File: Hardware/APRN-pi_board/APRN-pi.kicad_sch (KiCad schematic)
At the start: 30 parts, among them J1 Raspberry_Pi_2_3, J2 Conn_Coaxial, J3 Amplifier Jumper, J4 Screw_Terminal_01x02, J5 AudioJack4, Q1 MMBT3906, U1 DRA818V, U2 L7805

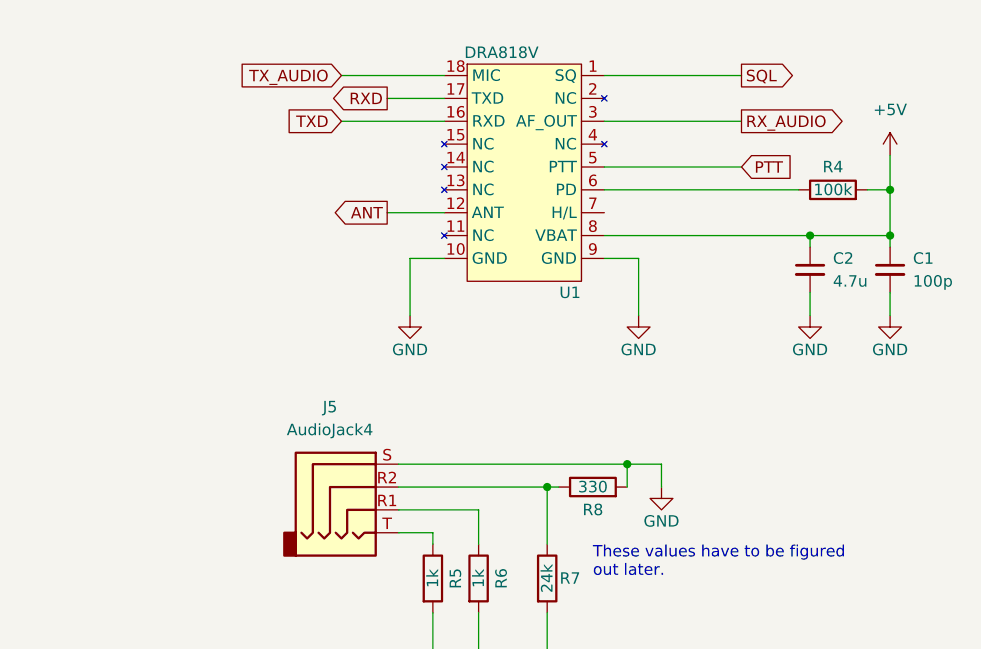
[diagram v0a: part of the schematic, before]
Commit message: Add h/l jumper
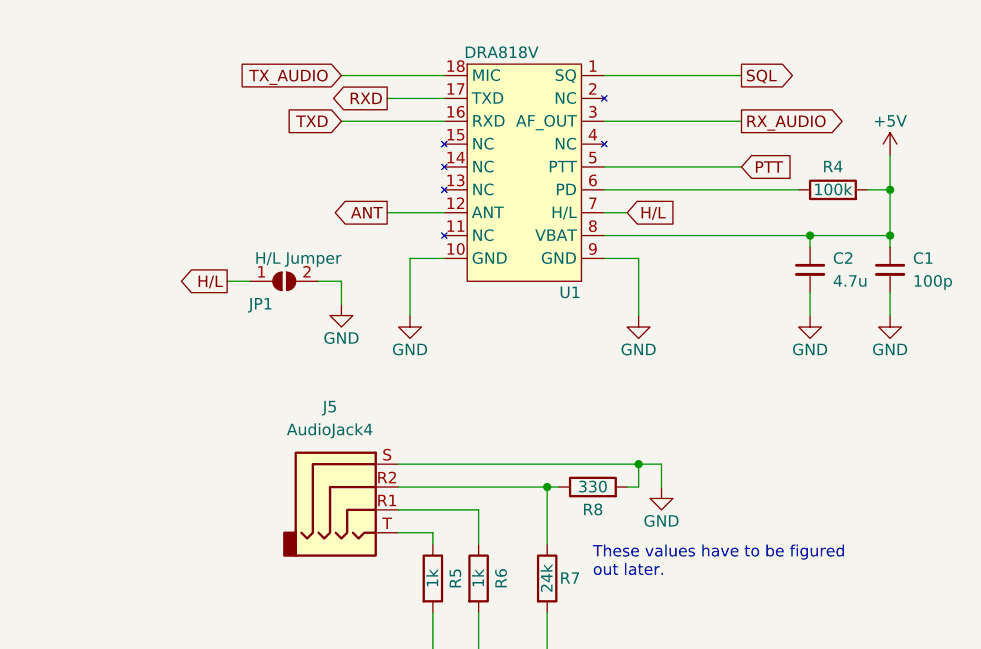
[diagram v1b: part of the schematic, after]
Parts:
- added JP1: H/L Jumper, Jumper:SolderJumper-2_P1.3mm_Open_TrianglePad1.0x1.5mm, symbol Jumper:SolderJumper_2_Open
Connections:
- net GND: now also JP1.2 (B)
- net H/L: now reaches U1.7 (H/L)
- net H/L: now also JP1.1 (A)
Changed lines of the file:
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@@
   (junction (at 76.2 97.79) (diameter 0) (color 0 0 0 0)
   )
-  (junction (at 245.11 64.77) (diameter 0) (color 0 0 0 0)
-  )
   (junction (at 33.02 97.79) (diameter 0) (color 0 0 0 0)
   )
@@
   )
   (junction (at 152.4 68.58) (diameter 0) (color 0 0 0 0)
+  )
+  (junction (at 246.38 64.77) (diameter 0) (color 0 0 0 0)
   )
   (junction (at 265.43 39.37) (diameter 0) (color 0 0 0 0)
@@
     (stroke (width 0) (type default) (color 0 0 0 0))
   )
+  (wire (pts (xy 246.38 64.77) (xy 248.92 64.77))
+    (stroke (width 0) (type default) (color 0 0 0 0))
+  )
   (wire (pts (xy 40.64 24.13) (xy 48.26 24.13))
     (stroke (width 0) (type default) (color 0 0 0 0))
@@
     (stroke (width 0) (type default) (color 0 0 0 0))
   )
+  (wire (pts (xy 242.57 36.83) (xy 245.11 36.83))
+    (stroke (width 0) (type default) (color 0 0 0 0))
+  )
   (wire (pts (xy 213.36 21.59) (xy 224.79 21.59))
     (stroke (width 0) (type default) (color 0 0 0 0))
@@
     (stroke (width 0) (type default) (color 0 0 0 0))
   )
-  (wire (pts (xy 219.71 64.77) (xy 245.11 64.77))
-    (stroke (width 0) (type default) (color 0 0 0 0))
-  )
   (wire (pts (xy 76.2 121.92) (xy 82.55 121.92))
     (stroke (width 0) (type default) (color 0 0 0 0))
@@
     (stroke (width 0) (type default) (color 0 0 0 0))
   )
+  (wire (pts (xy 213.36 44.45) (xy 213.36 46.99))
+    (stroke (width 0) (type default) (color 0 0 0 0))
+  )
   (wire (pts (xy 154.94 139.7) (xy 160.02 139.7))
     (stroke (width 0) (type default) (color 0 0 0 0))
@@
     (stroke (width 0) (type default) (color 0 0 0 0))
   )
+  (wire (pts (xy 210.82 44.45) (xy 213.36 44.45))
+    (stroke (width 0) (type default) (color 0 0 0 0))
+  )
   (wire (pts (xy 242.57 39.37) (xy 265.43 39.37))
     (stroke (width 0) (type default) (color 0 0 0 0))
@@
     (stroke (width 0) (type default) (color 0 0 0 0))
   )
+  (wire (pts (xy 246.38 67.31) (xy 245.11 67.31))
+    (stroke (width 0) (type default) (color 0 0 0 0))
+  )
   (wire (pts (xy 144.78 68.58) (xy 142.24 68.58))
     (stroke (width 0) (type default) (color 0 0 0 0))
@@
     (stroke (width 0) (type default) (color 0 0 0 0))
   )
+  (wire (pts (xy 219.71 64.77) (xy 246.38 64.77))
+    (stroke (width 0) (type default) (color 0 0 0 0))
+  )
   (wire (pts (xy 242.57 34.29) (xy 264.16 34.29))
     (stroke (width 0) (type default) (color 0 0 0 0))
@@
     (stroke (width 0) (type default) (color 0 0 0 0))
   )
-  (wire (pts (xy 245.11 64.77) (xy 248.92 64.77))
-    (stroke (width 0) (type default) (color 0 0 0 0))
-  )
   (wire (pts (xy 64.77 121.92) (xy 76.2 121.92))
     (stroke (width 0) (type default) (color 0 0 0 0))
@@
     (stroke (width 0) (type default) (color 0 0 0 0))
   )
-  (wire (pts (xy 245.11 64.77) (xy 245.11 67.31))
+  (wire (pts (xy 246.38 64.77) (xy 246.38 67.31))
+    (stroke (width 0) (type default) (color 0 0 0 0))
+  )
+  (wire (pts (xy 200.66 44.45) (xy 203.2 44.45))
     (stroke (width 0) (type default) (color 0 0 0 0))
   )
@@
     )
   )
+  (global_label "H{slash}L" (shape input) (at 245.11 36.83 0) (fields_autoplaced)
+    (effects (font (size 1.27 1.27)) (justify left))
+    (property "Intersheet References" "${INTERSHEET_REFS}" (id 0) (at 251.2121 36.7506 0)
+      (effects (font (size 1.27 1.27)) (justify left) hide)
+    )
+  )
   (global_label "PTT" (shape input) (at 257.81 31.75 0) (fields_autoplaced)
     (effects (font (size 1.27 1.27)) (justify left))
@@
     (effects (font (size 1.27 1.27)) (justify right))
     (property "Intersheet References" "${INTERSHEET_REFS}" (id 0) (at 212.6402 36.9094 0)
+      (effects (font (size 1.27 1.27)) (justify right) hide)
+    )
+  )
+  (global_label "H{slash}L" (shape output) (at 200.66 44.45 180) (fields_autoplaced)
+    (effects (font (size 1.27 1.27)) (justify right))
+    (property "Intersheet References" "${INTERSHEET_REFS}" (id 0) (at 194.5579 44.3706 0)
       (effects (font (size 1.27 1.27)) (justify right) hide)
     )
@@
   )
   (symbol (lib_id "power:+5V") (at 274.32 30.48 0) (unit 1)
-    (in_bom yes) (on_board yes) (fields_autoplaced)
+    (in_bom yes) (on_board yes)
     (property "Reference" "#PWR0104" (id 0) (at 274.32 34.29 0)
       (effects (font (size 1.27 1.27)) hide)
     )
-    (property "Value" "+5V" (id 1) (at 274.32 25.4 0))
+    (property "Value" "+5V" (id 1) (at 274.32 26.67 0))
     (property "Footprint" "" (id 2) (at 274.32 30.48 0)
       (effects (font (size 1.27 1.27)) hide)
@@
     (pin "1")
   )
+  (symbol (lib_id "Jumper:SolderJumper_2_Open") (at 207.01 44.45 0) (unit 1)
+    (in_bom yes) (on_board yes)
+    (property "Reference" "JP1" (id 0) (at 205.74 46.99 0)
+      (effects (font (size 1.27 1.27)) (justify right))
+    )
+    (property "Value" "H/L Jumper" (id 1) (at 213.36 41.91 0)
+      (effects (font (size 1.27 1.27)) (justify right))
+    )
+    (property "Footprint" "Jumper:SolderJumper-2_P1.3mm_Open_TrianglePad1.0x1.5mm" (id 2) (at 207.01 44.45 0)
+      (effects (font (size 1.27 1.27)) hide)
+    )
+    (property "Datasheet" "~" (id 3) (at 207.01 44.45 0)
+      (effects (font (size 1.27 1.27)) hide)
+    )
+    (pin "1")
+    (pin "2")
+  )
   (symbol (lib_id "Device:R") (at 50.8 97.79 90) (unit 1)
     (in_bom yes) (on_board yes)
@@
     )
     (property "Datasheet" "" (id 3) (at 220.98 48.26 0)
+      (effects (font (size 1.27 1.27)) hide)
+    )
+    (pin "1")
+  )
+  (symbol (lib_id "power:GND") (at 213.36 46.99 0) (unit 1)
+    (in_bom yes) (on_board yes)
+    (property "Reference" "#PWR01" (id 0) (at 213.36 53.34 0)
+      (effects (font (size 1.27 1.27)) hide)
+    )
+    (property "Value" "GND" (id 1) (at 213.36 50.8 0))
+    (property "Footprint" "" (id 2) (at 213.36 46.99 0)
+      (effects (font (size 1.27 1.27)) hide)
+    )
+    (property "Datasheet" "" (id 3) (at 213.36 46.99 0)
       (effects (font (size 1.27 1.27)) hide)
     )
@@
   )
   (symbol_instances
+    (path "/7a4a7cd3-b322-4799-bd04-d77279f4cccb"
+      (reference "#PWR01") (unit 1) (value "GND") (footprint "")
+    )
     (path "/154d3377-6296-4aab-9aa3-3cabfc82996f"
       (reference "#PWR0101") (unit 1) (value "GND") (footprint "")
@@
       (reference "J5") (unit 1) (value "AudioJack4") (footprint "Connector_Audio:Jack_3.5mm_PJ320E_Horizontal")
     )
+    (path "/67106f57-015d-42ff-af4d-a495d14e3d9c"
+      (reference "JP1") (unit 1) (value "H/L Jumper") (footprint "Jumper:SolderJumper-2_P1.3mm_Open_TrianglePad1.0x1.5mm")
+    )
     (path "/934fbbb7-68d4-48b2-b966-8b80b47dd229"

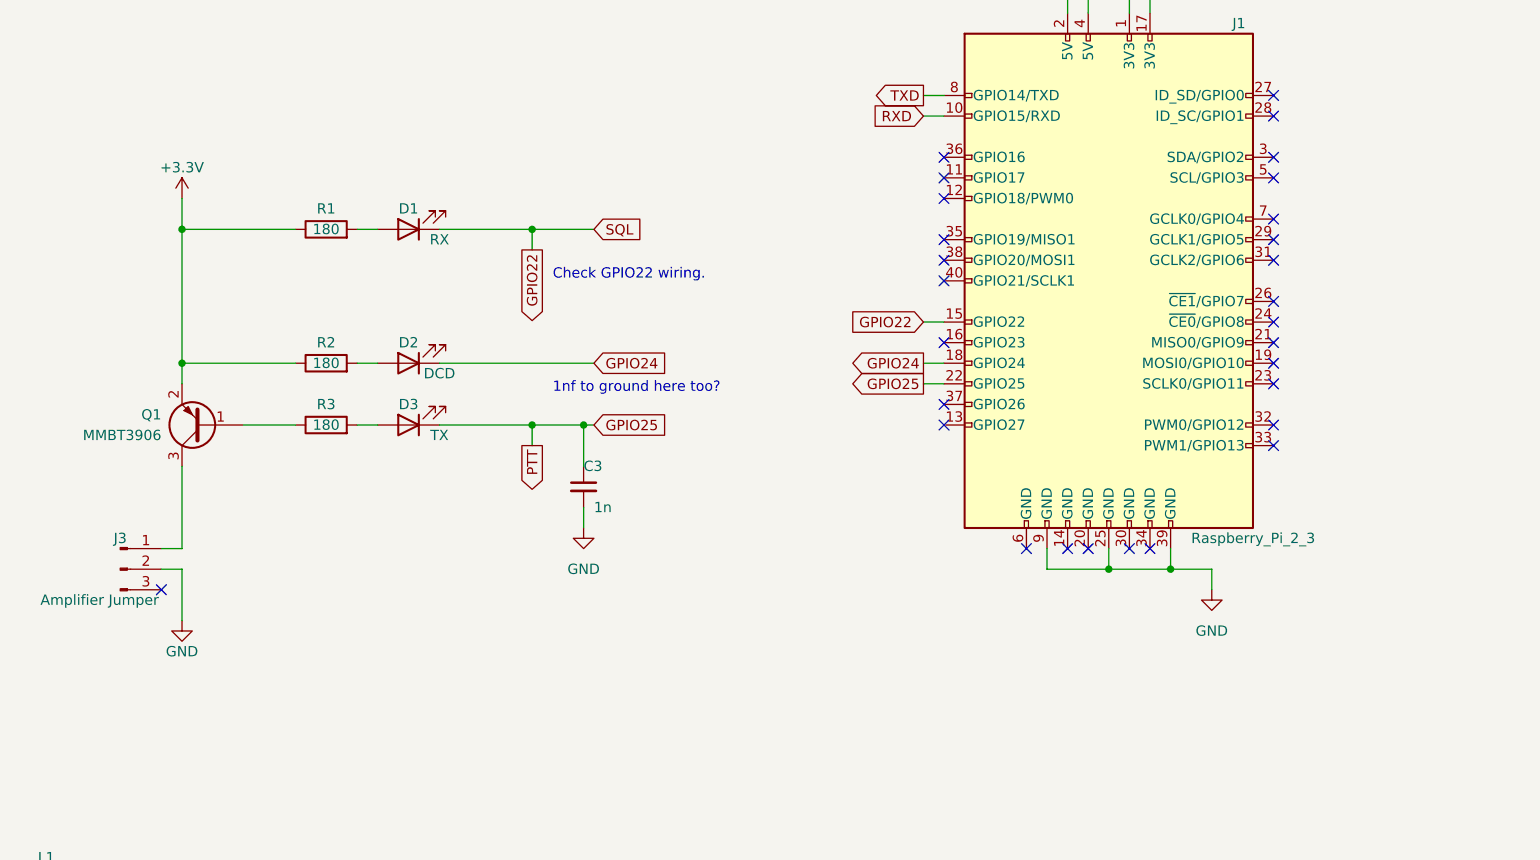
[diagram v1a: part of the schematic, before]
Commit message: add i2c breakout
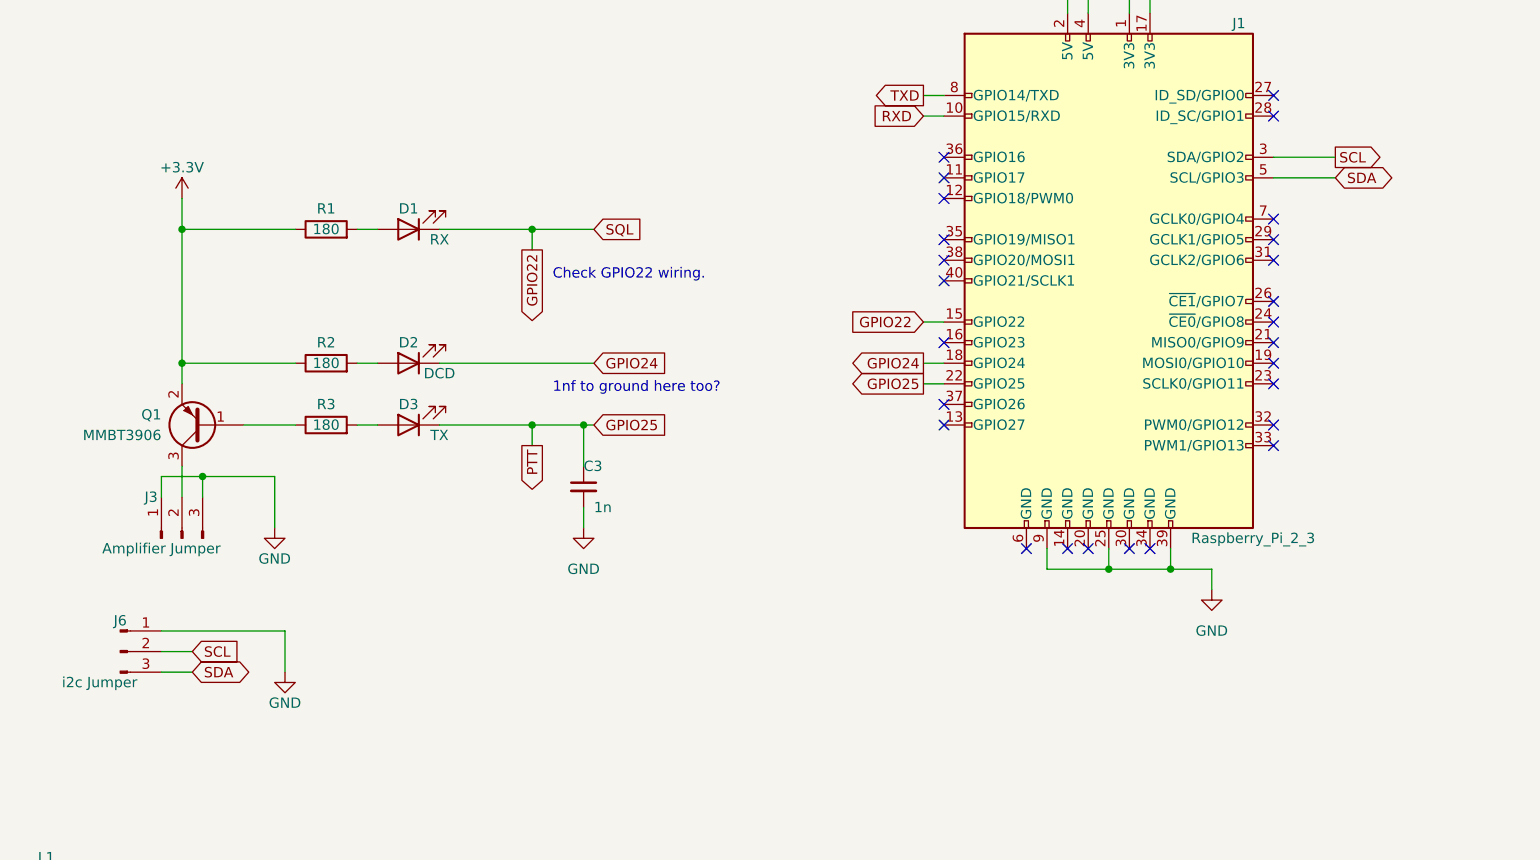
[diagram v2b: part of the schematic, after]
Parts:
- added J6: i2c Jumper, Connector_PinHeader_2.54mm:PinHeader_1x03_P2.54mm_Vertical, symbol Connector:Conn_01x03_Male
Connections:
- net GND: now also J3.1 (Pin_1), J3.3 (Pin_3), J6.1 (Pin_1); no longer J3.2 (Pin_2)
- net at Q1.3 (C): now also J3.2 (Pin_2); no longer J3.1 (Pin_1)
- net SCL: now reaches J1.3 (SDA/GPIO2)
- net SCL: now also J6.2 (Pin_2)
- net SDA: now reaches J1.5 (SCL/GPIO3)
- net SDA: now also J6.3 (Pin_3)
- no-connect marks 29 -> 26
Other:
- moved on the sheet: J3

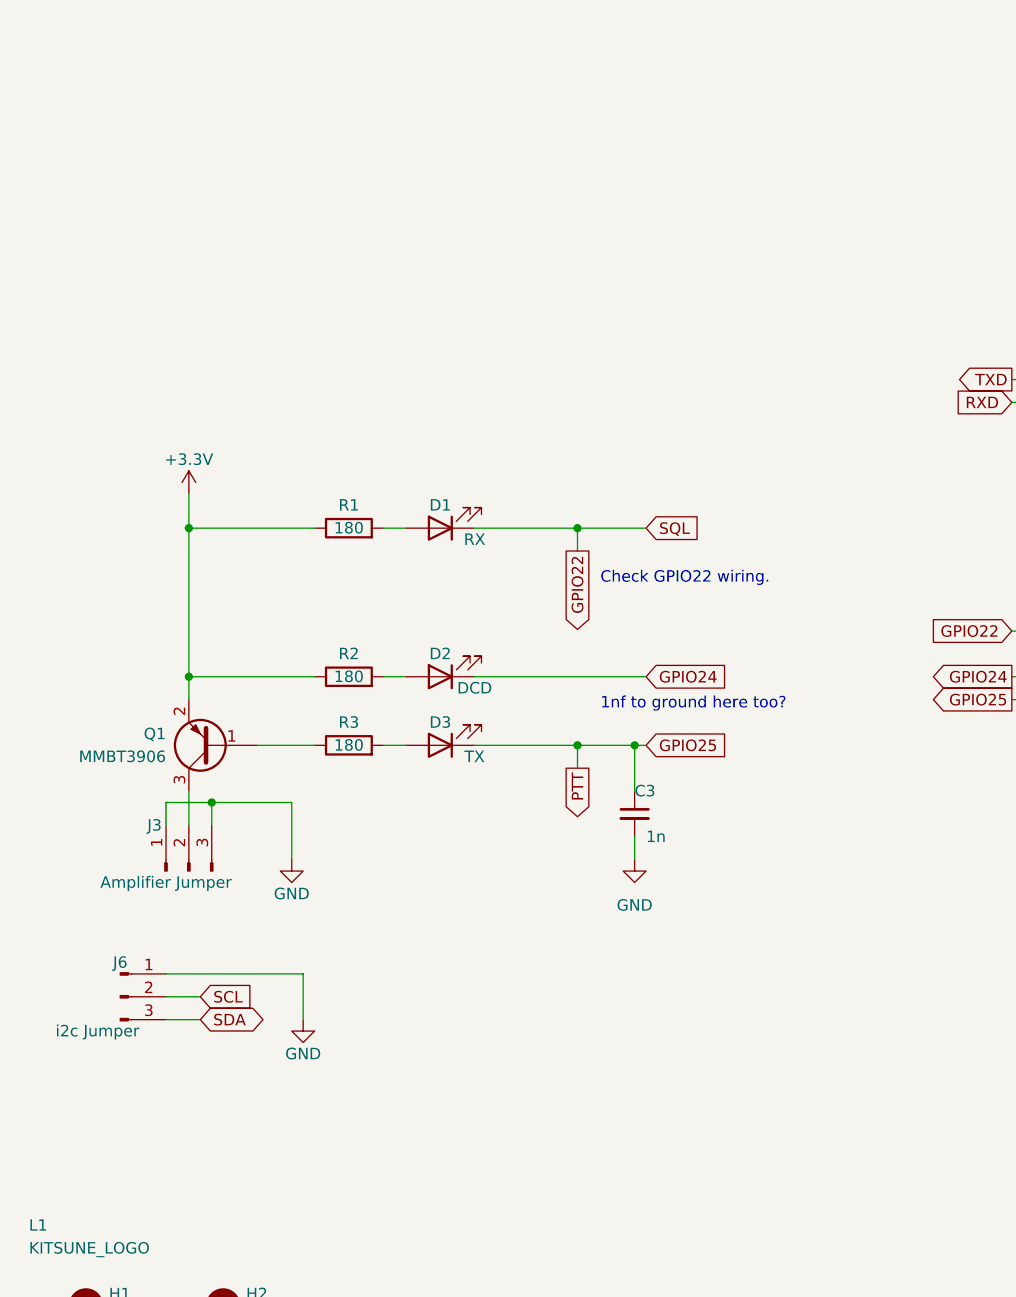
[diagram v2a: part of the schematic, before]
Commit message: This board will tottally need a rewiring
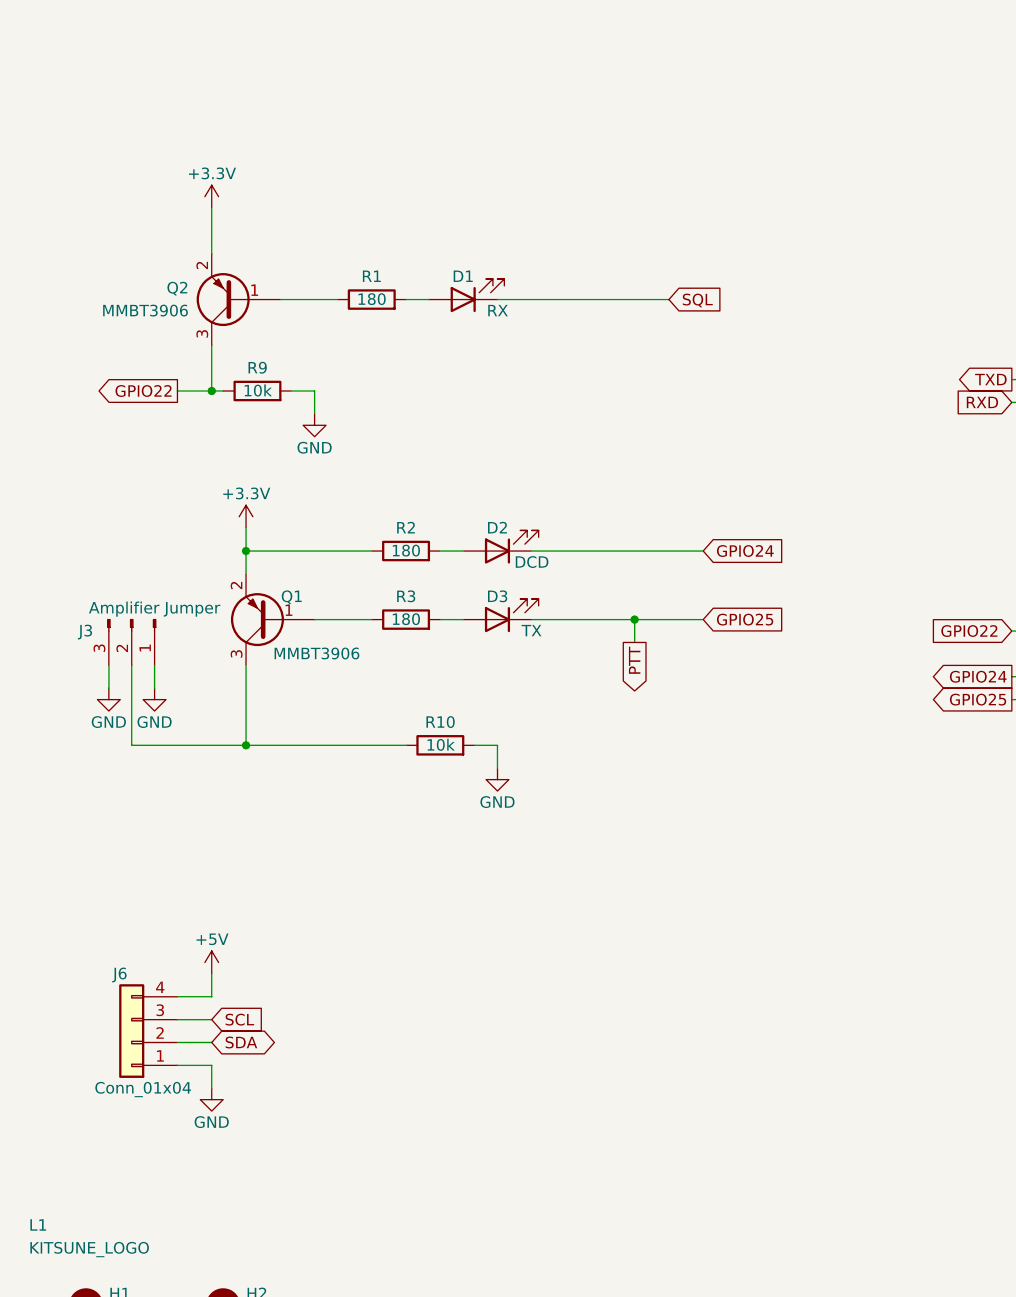
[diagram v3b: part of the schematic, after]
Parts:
- removed C3: 1n, Capacitor_SMD:C_0805_2012Metric, symbol Device:C_Small
- removed J6: i2c Jumper, Connector_PinHeader_2.54mm:PinHeader_1x03_P2.54mm_Vertical, symbol Connector:Conn_01x03_Male
- added J6: Conn_01x04, Connector_PinHeader_2.54mm:PinHeader_1x04_P2.54mm_Vertical, symbol Connector_Generic:Conn_01x04
- added Q2: MMBT3906, Package_TO_SOT_SMD:SOT-23, symbol Transistor_BJT:MMBT3906
- added R10, R9: 10k, Resistor_SMD:R_0805_2012Metric, symbol Device:R
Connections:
- net +3V3: now also Q2.2 (E); no longer R1.1
- net +5V: now also J6.4 (Pin_4)
- net GND: now also J6.1 (Pin_1), R10.2, R9.2
- net GPIO22: now also Q2.3 (C), R9.1; no longer D1.1 (K), U1.1 (SQ)
- net SCL: now also J6.3 (Pin_3)
- net SDA: now also J6.2 (Pin_2)
- net at J3.2 (Pin_2), Q1.3 (C): now also R10.1
- new net: Q2.1 (B), R1.1
- new net SQL: D1.1 (K), U1.1 (SQ)
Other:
- note removed: "1nf to ground here too?"
- note removed: "Check GPIO22 wiring."
- moved on the sheet: D1, D2, D3, J3, Q1, R1, R2, R3

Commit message: misc
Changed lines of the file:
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@@
   (symbol (lib_id "Connector:Screw_Terminal_01x02") (at 26.67 26.67 180) (unit 1)
     (in_bom yes) (on_board yes)
-    (property "Reference" "J4" (id 0) (at 26.67 29.21 0))
-    (property "Value" "Screw_Terminal_01x02" (id 1) (at 26.67 21.59 0))
-    (property "Footprint" "TerminalBlock:TerminalBlock_bornier-2_P5.08mm" (id 2) (at 26.67 26.67 0)
+    (property "Reference" "J4" (id 0) (at 25.4 21.59 0))
+    (property "Value" "Screw_Terminal_01x02" (id 1) (at 24.13 29.21 0))
+    (property "Footprint" "TerminalBlock:TerminalBlock_bornier-2_P5.08mm" (id 2) (at 26.67 29.845 0)
       (effects (font (size 1.27 1.27)) hide)
     )
